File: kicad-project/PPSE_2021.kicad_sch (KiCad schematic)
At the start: 0 parts

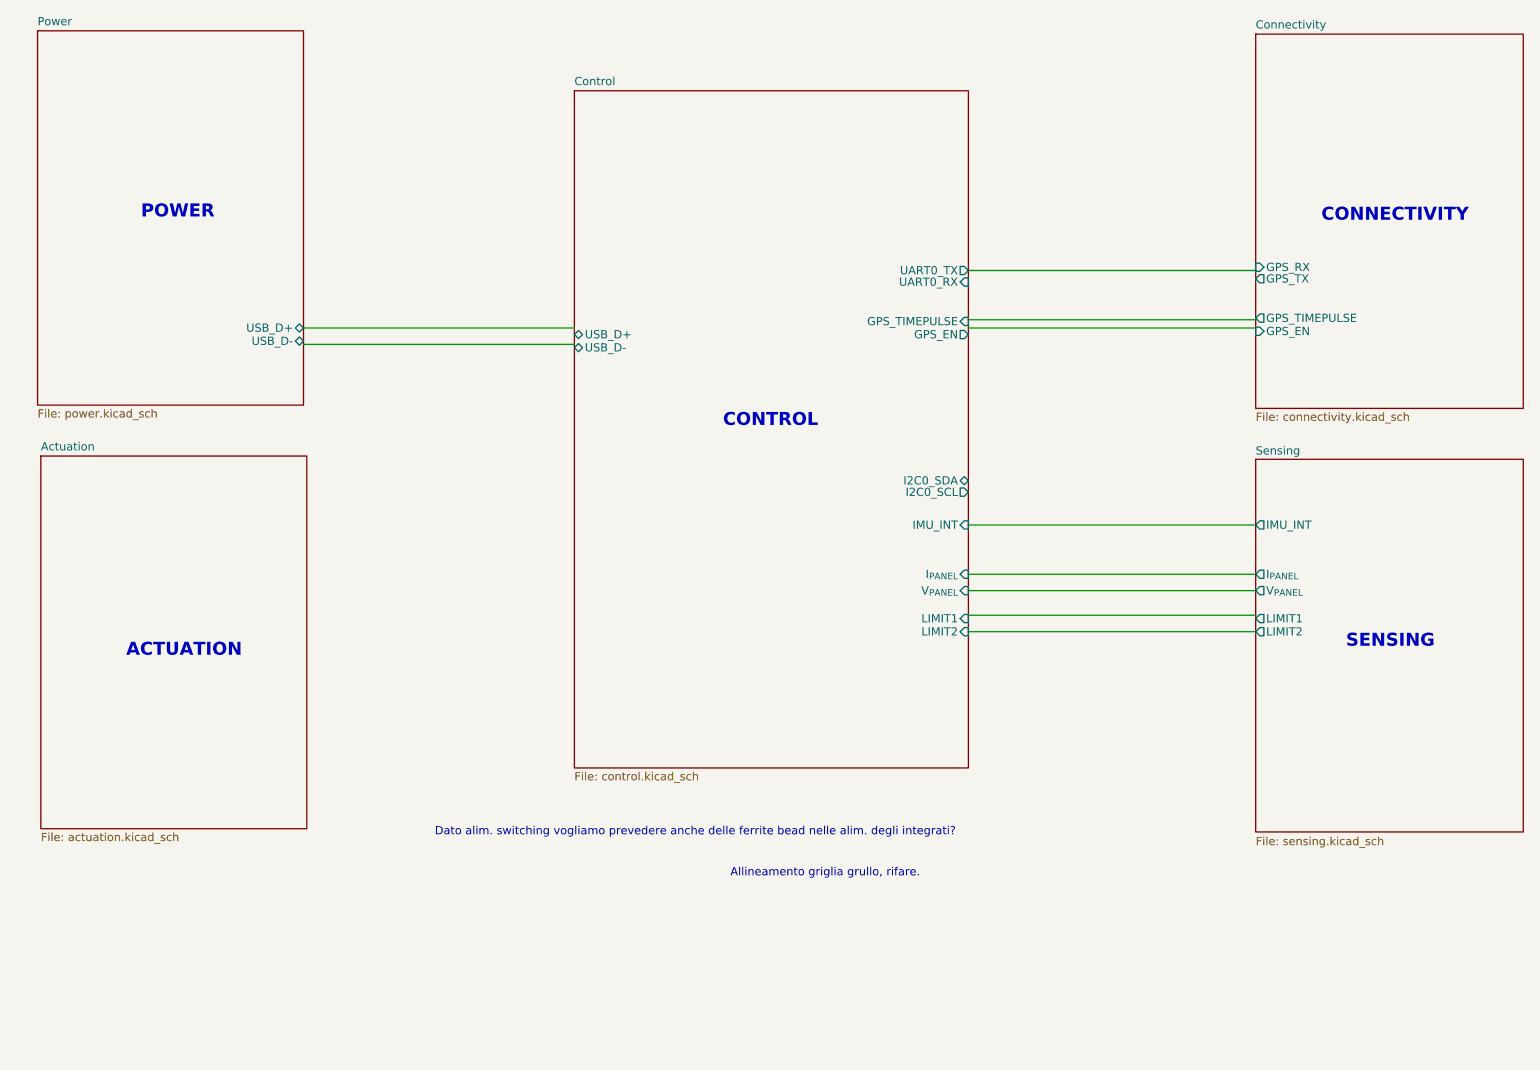
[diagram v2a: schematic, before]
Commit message: hw: set grid to 50 mils and missing labels
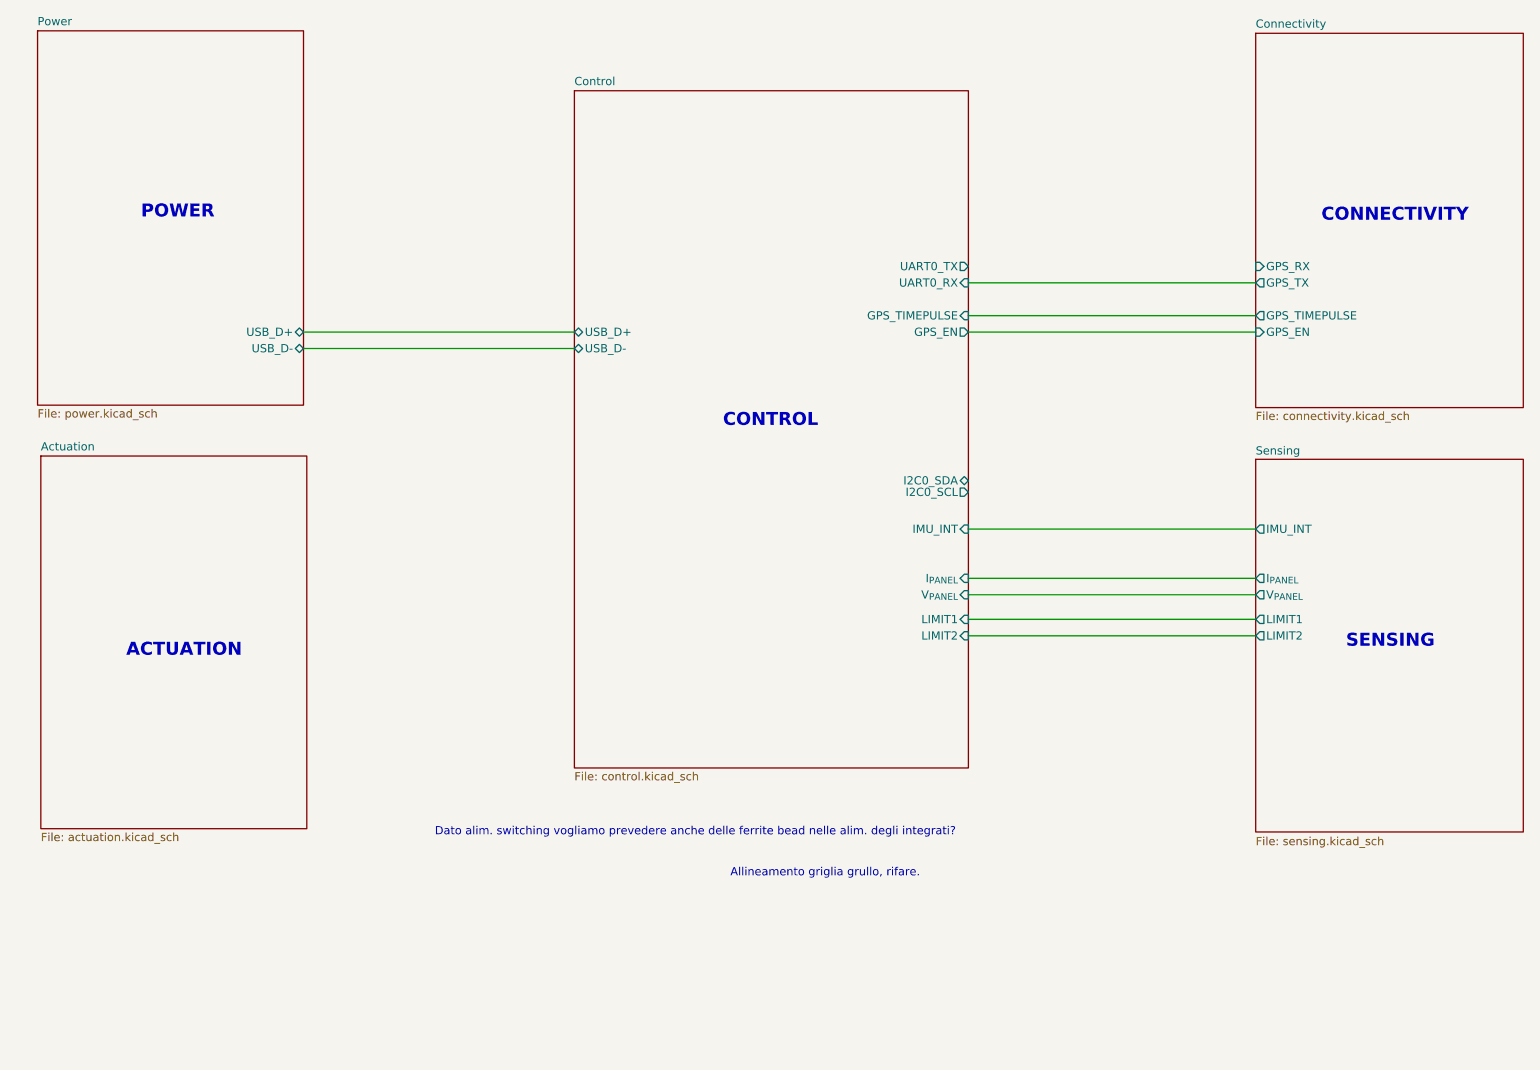
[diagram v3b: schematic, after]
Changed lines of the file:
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@@
     (title "Main")
   )
-  (wire (pts (xy 173.99 61.595) (xy 218.44 61.595))
-    (stroke (width 0) (type default) (color 0 0 0 0))
-  )
-  (wire (pts (xy 173.99 93.345) (xy 218.44 93.345))
-    (stroke (width 0) (type default) (color 0 0 0 0))
-  )
-  (wire (pts (xy 173.99 100.965) (xy 218.44 100.965))
-    (stroke (width 0) (type default) (color 0 0 0 0))
-  )
-  (wire (pts (xy 173.99 53.975) (xy 218.44 53.975))
-    (stroke (width 0) (type default) (color 0 0 0 0))
-  )
-  (wire (pts (xy 218.44 62.865) (xy 173.99 62.865))
-    (stroke (width 0) (type default) (color 0 0 0 0))
-  )
-  (wire (pts (xy 173.99 103.505) (xy 218.44 103.505))
-    (stroke (width 0) (type default) (color 0 0 0 0))
-  )
-  (wire (pts (xy 71.12 65.405) (xy 113.03 65.405))
-    (stroke (width 0) (type default) (color 0 0 0 0))
-  )
-  (wire (pts (xy 71.12 62.865) (xy 113.03 62.865))
-    (stroke (width 0) (type default) (color 0 0 0 0))
-  )
-  (wire (pts (xy 173.99 109.855) (xy 218.44 109.855))
-    (stroke (width 0) (type default) (color 0 0 0 0))
-  )
-  (wire (pts (xy 173.99 107.315) (xy 218.44 107.315))
+  (wire (pts (xy 71.12 63.5) (xy 113.03 63.5))
+    (stroke (width 0) (type default) (color 0 0 0 0))
+  )
+  (wire (pts (xy 173.99 107.95) (xy 218.44 107.95))
+    (stroke (width 0) (type default) (color 0 0 0 0))
+  )
+  (wire (pts (xy 173.99 60.96) (xy 218.44 60.96))
+    (stroke (width 0) (type default) (color 0 0 0 0))
+  )
+  (wire (pts (xy 173.99 55.88) (xy 218.44 55.88))
+    (stroke (width 0) (type default) (color 0 0 0 0))
+  )
+  (wire (pts (xy 173.99 104.14) (xy 218.44 104.14))
+    (stroke (width 0) (type default) (color 0 0 0 0))
+  )
+  (wire (pts (xy 218.44 63.5) (xy 173.99 63.5))
+    (stroke (width 0) (type default) (color 0 0 0 0))
+  )
+  (wire (pts (xy 173.99 110.49) (xy 218.44 110.49))
+    (stroke (width 0) (type default) (color 0 0 0 0))
+  )
+  (wire (pts (xy 173.99 93.98) (xy 218.44 93.98))
+    (stroke (width 0) (type default) (color 0 0 0 0))
+  )
+  (wire (pts (xy 173.99 101.6) (xy 218.44 101.6))
+    (stroke (width 0) (type default) (color 0 0 0 0))
+  )
+  (wire (pts (xy 71.12 66.04) (xy 113.03 66.04))
     (stroke (width 0) (type default) (color 0 0 0 0))
   )
@@
       (effects (font (size 1.27 1.27)) (justify left top))
     )
-    (pin "GPS_EN" output (at 173.99 63.881 0)
-      (effects (font (size 1.27 1.27)) (justify right))
-    )
-    (pin "GPS_TIMEPULSE" input (at 173.99 61.849 0)
+    (pin "GPS_EN" output (at 173.99 63.5 0)
+      (effects (font (size 1.27 1.27)) (justify right))
+    )
+    (pin "GPS_TIMEPULSE" input (at 173.99 60.96 0)
       (effects (font (size 1.27 1.27)) (justify right))
     )
@@
       (effects (font (size 1.27 1.27)) (justify right))
     )
-    (pin "IMU_INT" input (at 173.99 93.345 0)
-      (effects (font (size 1.27 1.27)) (justify right))
-    )
-    (pin "UART0_TX" output (at 173.99 53.975 0)
+    (pin "IMU_INT" input (at 173.99 93.98 0)
+      (effects (font (size 1.27 1.27)) (justify right))
+    )
+    (pin "UART0_TX" output (at 173.99 53.34 0)
       (effects (font (size 1.27 1.27)) (justify right))
     )
@@
       (effects (font (size 1.27 1.27)) (justify right))
     )
-    (pin "UART0_RX" input (at 173.99 55.753 0)
-      (effects (font (size 1.27 1.27)) (justify right))
-    )
-    (pin "USB_D+" bidirectional (at 113.03 63.881 180)
-      (effects (font (size 1.27 1.27)) (justify left))
-    )
-    (pin "USB_D-" bidirectional (at 113.03 65.913 180)
-      (effects (font (size 1.27 1.27)) (justify left))
-    )
-    (pin "I_{PANEL}" input (at 173.99 100.965 0)
-      (effects (font (size 1.27 1.27)) (justify right))
-    )
-    (pin "V_{PANEL}" input (at 173.99 103.505 0)
-      (effects (font (size 1.27 1.27)) (justify right))
-    )
-    (pin "LIMIT1" input (at 173.99 107.823 0)
-      (effects (font (size 1.27 1.27)) (justify right))
-    )
-    (pin "LIMIT2" input (at 173.99 109.855 0)
-      (effects (font (size 1.27 1.27)) (justify right))
-    )
-  )
-  (sheet (at 218.44 17.399) (size 41.402 57.912) (fields_autoplaced)
+    (pin "UART0_RX" input (at 173.99 55.88 0)
+      (effects (font (size 1.27 1.27)) (justify right))
+    )
+    (pin "USB_D+" bidirectional (at 113.03 63.5 180)
+      (effects (font (size 1.27 1.27)) (justify left))
+    )
+    (pin "USB_D-" bidirectional (at 113.03 66.04 180)
+      (effects (font (size 1.27 1.27)) (justify left))
+    )
+    (pin "I_{PANEL}" input (at 173.99 101.6 0)
+      (effects (font (size 1.27 1.27)) (justify right))
+    )
+    (pin "V_{PANEL}" input (at 173.99 104.14 0)
+      (effects (font (size 1.27 1.27)) (justify right))
+    )
+    (pin "LIMIT1" input (at 173.99 107.95 0)
+      (effects (font (size 1.27 1.27)) (justify right))
+    )
+    (pin "LIMIT2" input (at 173.99 110.49 0)
+      (effects (font (size 1.27 1.27)) (justify right))
+    )
+  )
+  (sheet (at 218.44 17.272) (size 41.402 57.912) (fields_autoplaced)
     (stroke (width 0) (type solid) (color 0 0 0 0))
     (fill (color 0 0 0 0.0000))
-    (property "Sheet name" "Connectivity" (id 0) (at 218.44 16.6874 0)
+    (property "Sheet name" "Connectivity" (id 0) (at 218.44 16.5604 0)
       (effects (font (size 1.27 1.27)) (justify left bottom))
     )
-    (property "Sheet file" "connectivity.kicad_sch" (id 1) (at 218.44 75.8956 0)
+    (property "Sheet file" "connectivity.kicad_sch" (id 1) (at 218.44 75.7686 0)
       (effects (font (size 1.27 1.27)) (justify left top))
     )
-    (pin "GPS_RX" input (at 218.44 53.467 180)
-      (effects (font (size 1.27 1.27)) (justify left))
-    )
-    (pin "GPS_TX" output (at 218.44 55.245 180)
-      (effects (font (size 1.27 1.27)) (justify left))
-    )
-    (pin "GPS_EN" input (at 218.44 63.373 180)
-      (effects (font (size 1.27 1.27)) (justify left))
-    )
-    (pin "GPS_TIMEPULSE" output (at 218.44 61.341 180)
+    (pin "GPS_RX" input (at 218.44 53.34 180)
+      (effects (font (size 1.27 1.27)) (justify left))
+    )
+    (pin "GPS_TX" output (at 218.44 55.88 180)
+      (effects (font (size 1.27 1.27)) (justify left))
+    )
+    (pin "GPS_EN" input (at 218.44 63.5 180)
+      (effects (font (size 1.27 1.27)) (justify left))
+    )
+    (pin "GPS_TIMEPULSE" output (at 218.44 60.96 180)
       (effects (font (size 1.27 1.27)) (justify left))
     )
@@
       (effects (font (size 1.27 1.27)) (justify left top))
     )
-    (pin "USB_D+" bidirectional (at 71.12 62.865 0)
-      (effects (font (size 1.27 1.27)) (justify right))
-    )
-    (pin "USB_D-" bidirectional (at 71.12 64.897 0)
+    (pin "USB_D+" bidirectional (at 71.12 63.5 0)
+      (effects (font (size 1.27 1.27)) (justify right))
+    )
+    (pin "USB_D-" bidirectional (at 71.12 66.04 0)
       (effects (font (size 1.27 1.27)) (justify right))
     )
@@
       (effects (font (size 1.27 1.27)) (justify left top))
     )
-    (pin "IMU_INT" output (at 218.44 93.345 180)
-      (effects (font (size 1.27 1.27)) (justify left))
-    )
-    (pin "I_{PANEL}" output (at 218.44 100.965 180)
-      (effects (font (size 1.27 1.27)) (justify left))
-    )
-    (pin "V_{PANEL}" output (at 218.44 103.505 180)
-      (effects (font (size 1.27 1.27)) (justify left))
-    )
-    (pin "LIMIT1" output (at 218.44 107.823 180)
-      (effects (font (size 1.27 1.27)) (justify left))
-    )
-    (pin "LIMIT2" output (at 218.44 109.855 180)
+    (pin "IMU_INT" output (at 218.44 93.98 180)
+      (effects (font (size 1.27 1.27)) (justify left))
+    )
+    (pin "I_{PANEL}" output (at 218.44 101.6 180)
+      (effects (font (size 1.27 1.27)) (justify left))
+    )
+    (pin "V_{PANEL}" output (at 218.44 104.14 180)
+      (effects (font (size 1.27 1.27)) (justify left))
+    )
+    (pin "LIMIT1" output (at 218.44 107.95 180)
+      (effects (font (size 1.27 1.27)) (justify left))
+    )
+    (pin "LIMIT2" output (at 218.44 110.49 180)
       (effects (font (size 1.27 1.27)) (justify left))
     )
@@
       (reference "U?") (unit 1) (value "A4988SETTR-T") (footprint "QFN50P500X500X90-29N")
     )
-    (path "/755090ec-fdfb-40aa-83ce-f20a94352e8e/2a0dfdba-dc26-4b26-acb1-2e8f4f5ac3d7"
+    (path "/755090ec-fdfb-40aa-83ce-f20a94352e8e/5f9e161f-db30-44a1-a010-508bfbcccc5c"
       (reference "U?") (unit 1) (value "74AUC2G32") (footprint "")
     )

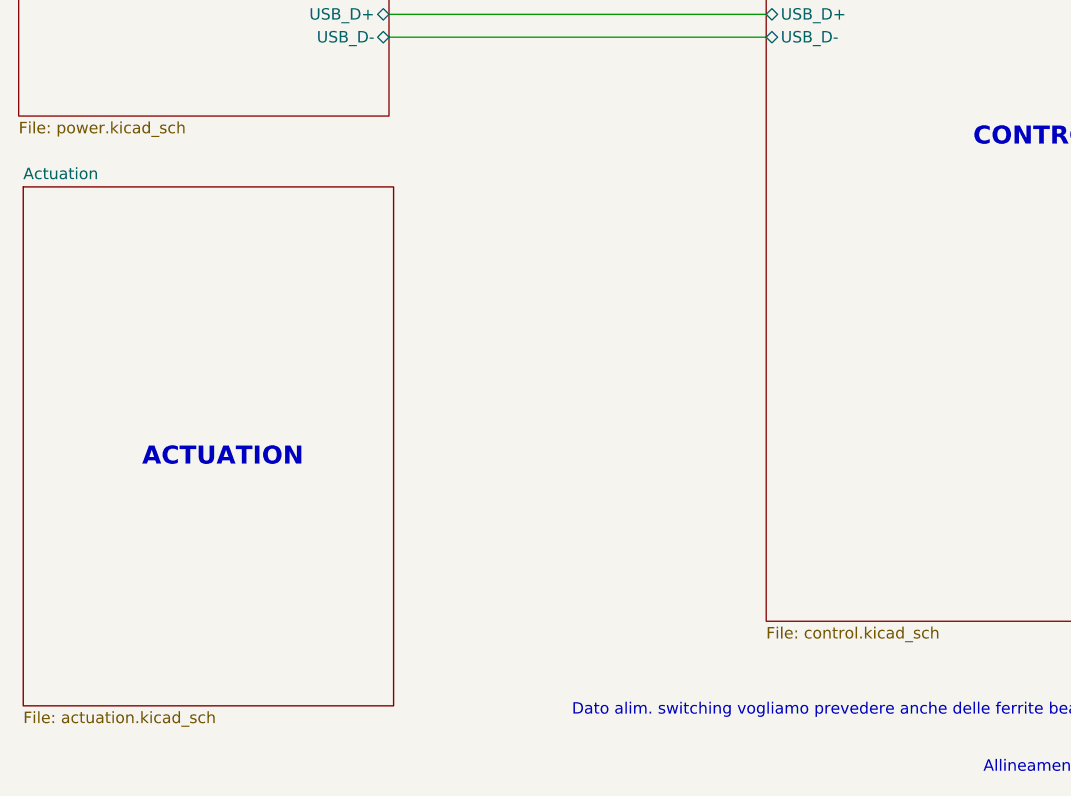
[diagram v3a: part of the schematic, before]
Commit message: hw: add stepper motor drivers
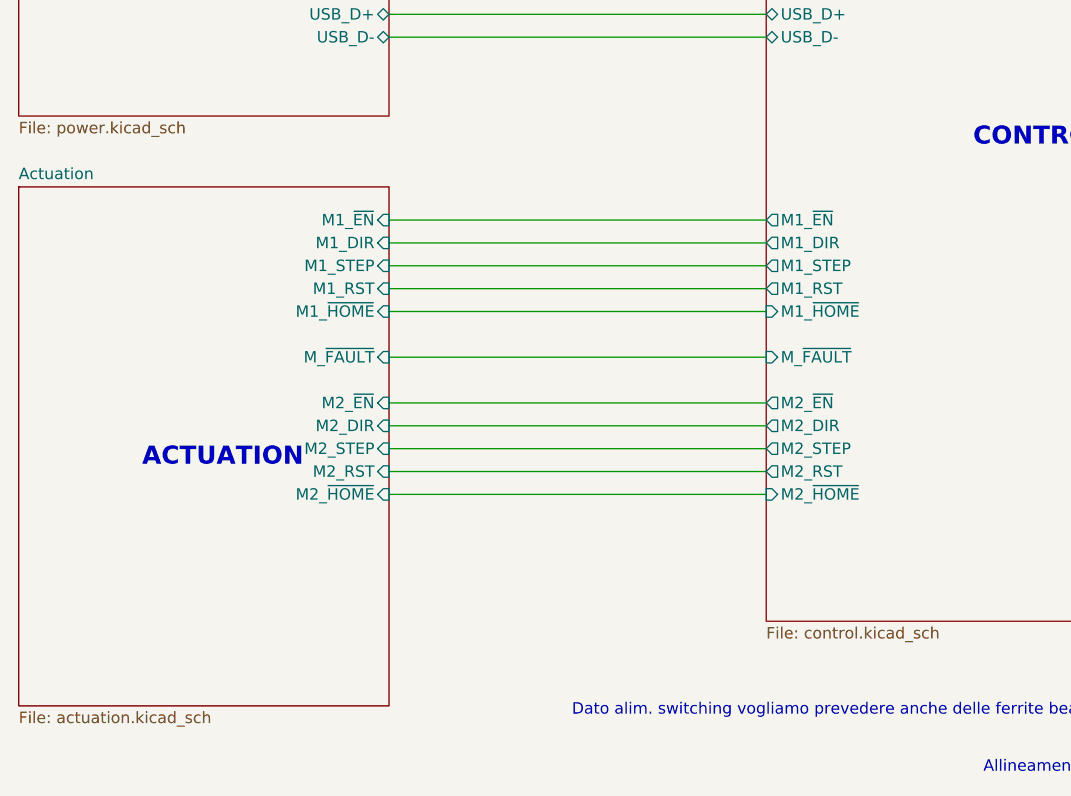
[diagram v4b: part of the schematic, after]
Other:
- sheet Actuation ports: added M1_DIR, M1_RST, M1_STEP, M1_~{EN}, M1_~{HOME}, M2_DIR, M2_RST, M2_STEP, M2_~{EN}, M2_~{HOME}, M_~{FAULT}; removed none
- sheet Control ports: added M1_DIR, M1_RST, M1_STEP, M1_~{EN}, M1_~{HOME}, M2_DIR, M2_RST, M2_STEP, M2_~{EN}, M2_~{HOME}, M_~{FAULT}; removed none

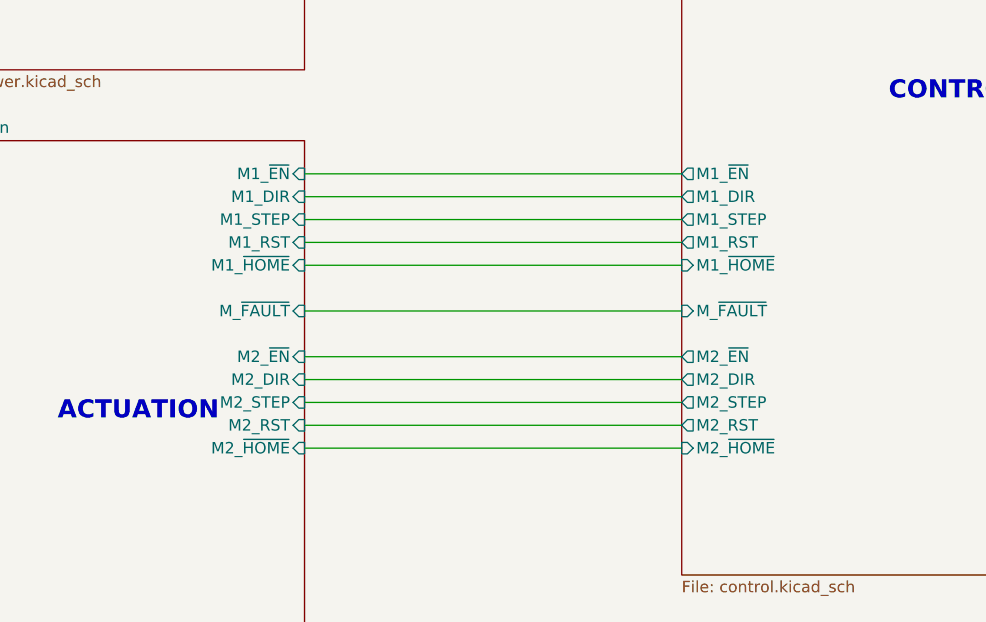
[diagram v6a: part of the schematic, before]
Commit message: fw: discrete dirver for stepper
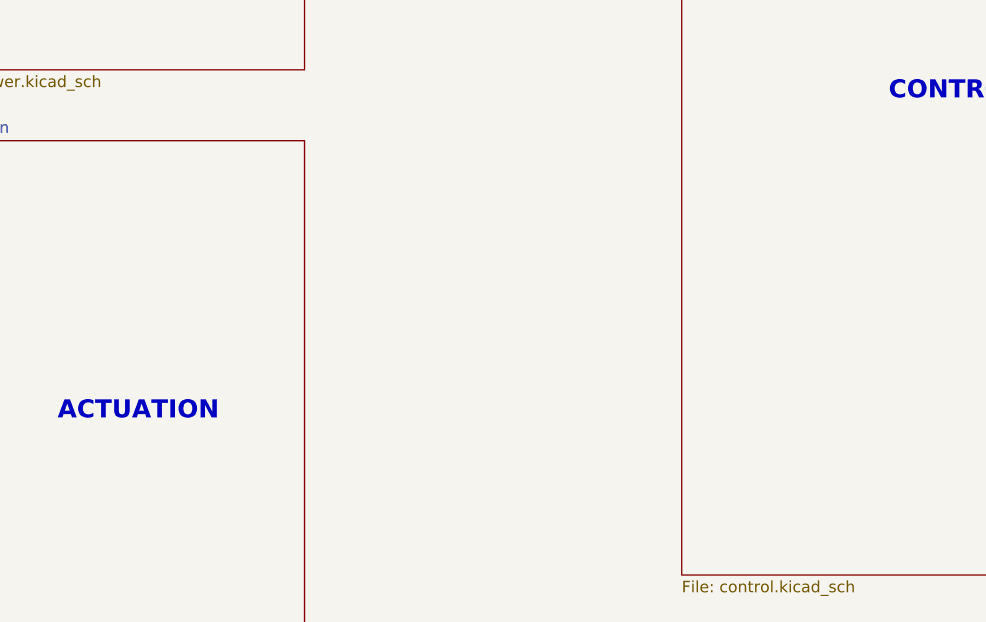
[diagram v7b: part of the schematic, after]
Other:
- sheet Actuation ports: added none; removed M1_DIR, M1_RST, M1_STEP, M1_~{EN}, M1_~{HOME}, M2_DIR, M2_RST, M2_STEP, M2_~{EN}, M2_~{HOME}, M_~{FAULT}
- sheet Control ports: added none; removed M1_DIR, M1_RST, M1_STEP, M1_~{EN}, M1_~{HOME}, M2_DIR, M2_RST, M2_STEP, M2_~{EN}, M2_~{HOME}, M_~{FAULT}
